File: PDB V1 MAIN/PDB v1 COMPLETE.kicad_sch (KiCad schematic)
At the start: 14 parts, among them J1 XT60PW-M, Q1 Q_NMOS, U1 TPS4800-Q1, U3 XT30PW-M, U4 XT30PW-M, U5 XT30PW-M, U6 XT30PW-M

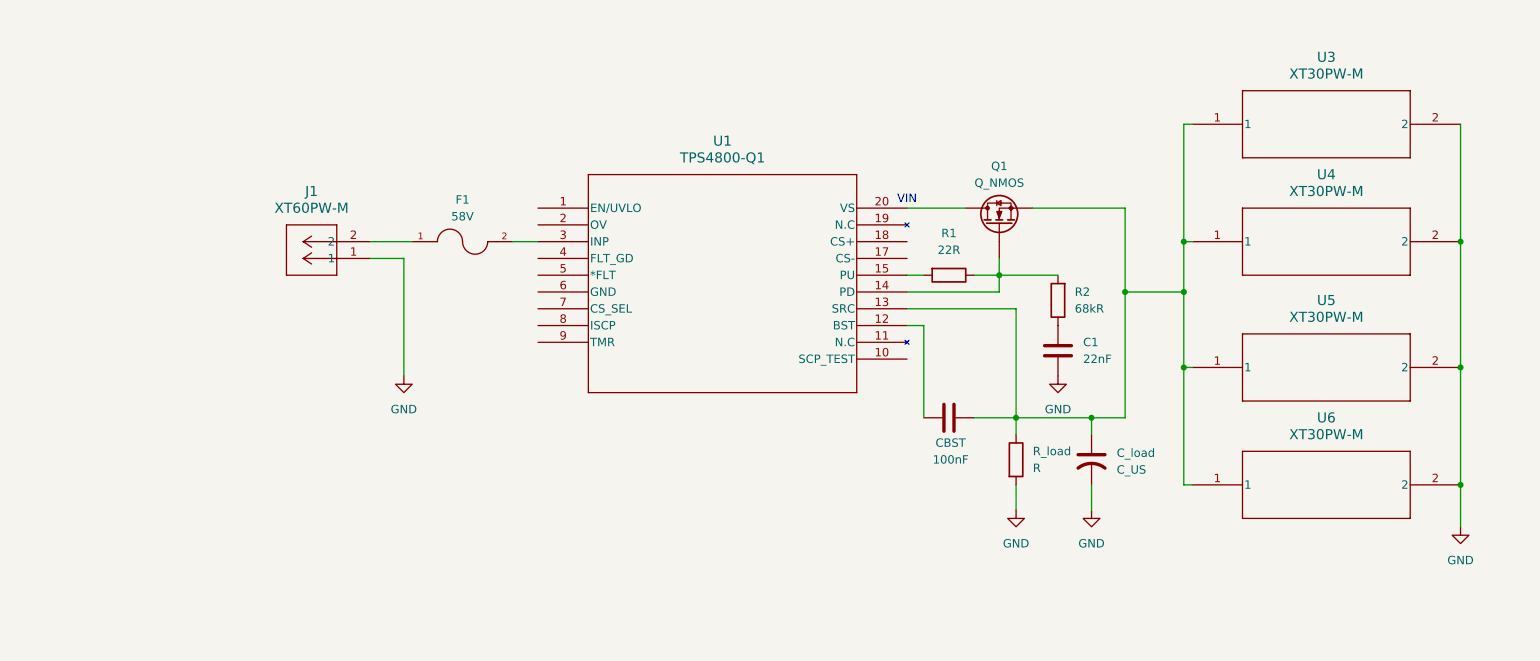
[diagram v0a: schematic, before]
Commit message: Pushing Last Weeks Changes/ Testing New Git Integration
I am pushing the previous weeks changes while testing out git for KiCad.
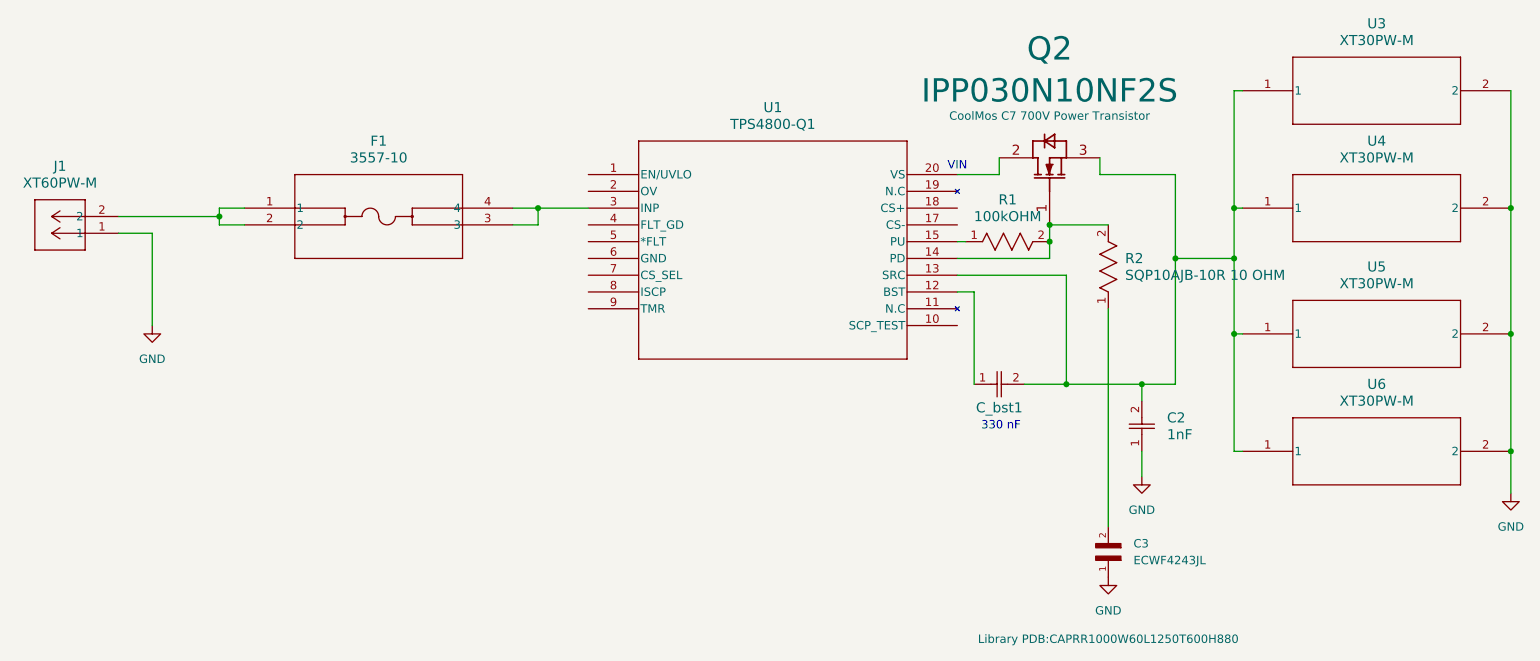
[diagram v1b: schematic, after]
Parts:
- removed C1: 22nF, symbol Device:C
- removed CBST: 100nF, symbol Device:C
- removed C_load: C_US, symbol Device:C_US
- removed F1: 58V, 3557-10:FUSE_3557-10, symbol 3557-10:3557-10
- removed Q1: Q_NMOS, symbol Device:Q_NMOS
- removed R1: 22R, symbol Device:R
- removed R2: 68kR, symbol Device:R
- removed R_load: R, symbol Device:R
- added C2: 1nF, Library PDB:CAP_16 X 25_PAN, symbol PDB SYMBOL LIBRARY:EEUFC1H102
- added C3: ECWF4243JL, Library PDB:CAPRR1000W60L1250T600H880, symbol PDB SYMBOL LIBRARY:ECWF4243JL
- added C_bst1: GRM32ER60G337ME05L, Library PDB:CAP_GRM32E_MUR, symbol PDB SYMBOL LIBRARY:GRM32ER60G337ME05L
- added F1: 3557-10, Library PDB:3557-10_KEY, symbol PDB SYMBOL LIBRARY:3557-10
- added Q2: IPP030N10NF2S, Library PDB:IFX-PG-TO220-3-60, symbol PDB SYMBOL LIBRARY:IPP030N10NF2S
- added R1: 100kOHM, Library PDB:RN60_VIS, symbol PDB SYMBOL LIBRARY:RN60D1003FB14
- added R2: SQP10AJB-10R 10 OHM, Library PDB:YAG_SQP10_YAG, symbol PDB SYMBOL LIBRARY:SQP10AJB-10R
- J1: footprint CONN_1805375_RSP -> Library PDB:CONN_1805375_RSP
- U1: footprint VSSOP19-DGX_TEX -> Library PDB:VSSOP19-DGX_TEX
- U3, U4, U5, U6: footprint XT30PW-M_AMA -> Library PDB:XT30PW-M_AMA
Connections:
- net GND: now also C2.1, C3.1
- net at J1.2: now also F1.1, F1.2
- net at U1.14 (PD): now also Q2.1 (GATE), R1.2, R2.2
- net at U1.15 (PU): now also R1.1
- net at U1.3 (INP): now also F1.3, F1.4
- net at U1.13 (SRC), U3.1, U4.1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: now also C2.2, C_bst1.2, Q2.3 (SOURCE)
- net at U1.20 (VS): now also Q2.2 (DRAIN)
- net at U1.12 (BST): now also C_bst1.1
- new net: C3.2, R2.1
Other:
- note added: "330 nF"
- moved on the sheet: J1, U1, U3, U4, U5, U6
